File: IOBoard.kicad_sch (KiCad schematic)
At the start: 45 parts, among them J1 Conn_02x05_Odd_Even, J10 Conn_02x05_Odd_Even, J11 Conn_02x05_Odd_Even, J2 Conn_02x05_Odd_Even, J3 Conn_01x03, J4 Conn_01x03, J5 Conn_01x03, J6 Conn_01x03, J7 Conn_01x03, J8 Conn_01x03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

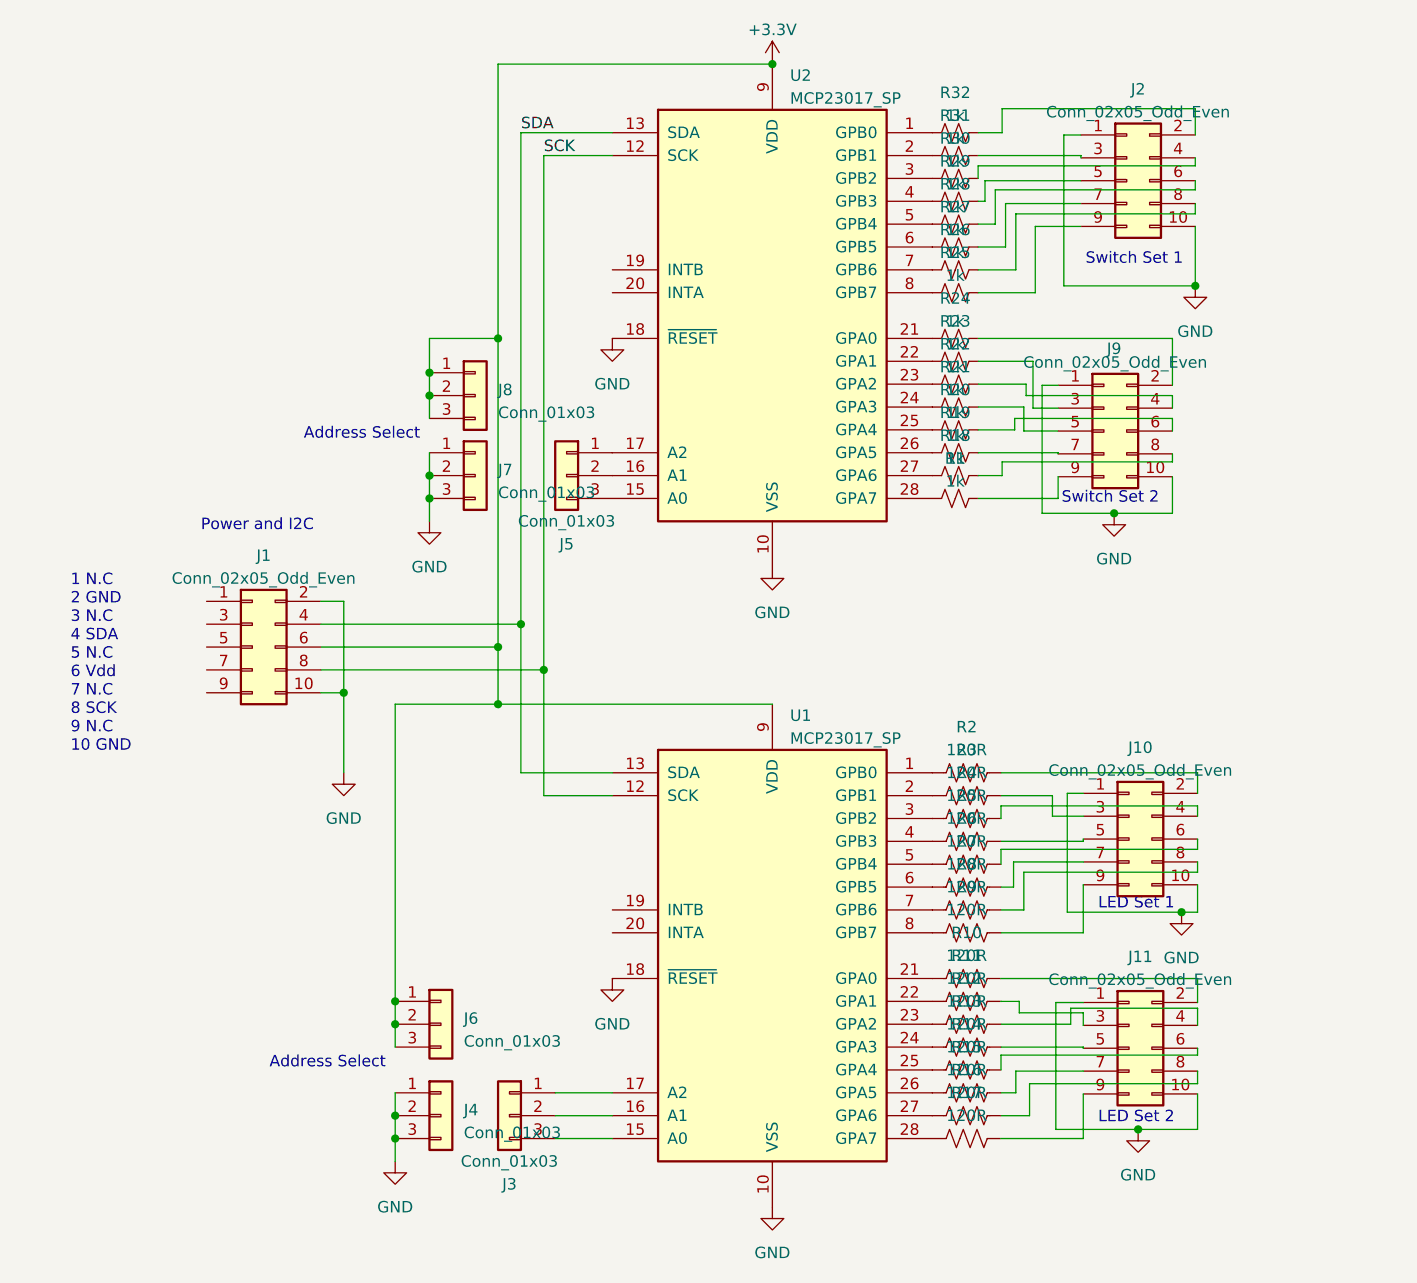
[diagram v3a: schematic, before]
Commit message: Fix schematic error and re-layout board.  Start a tray to hold board.
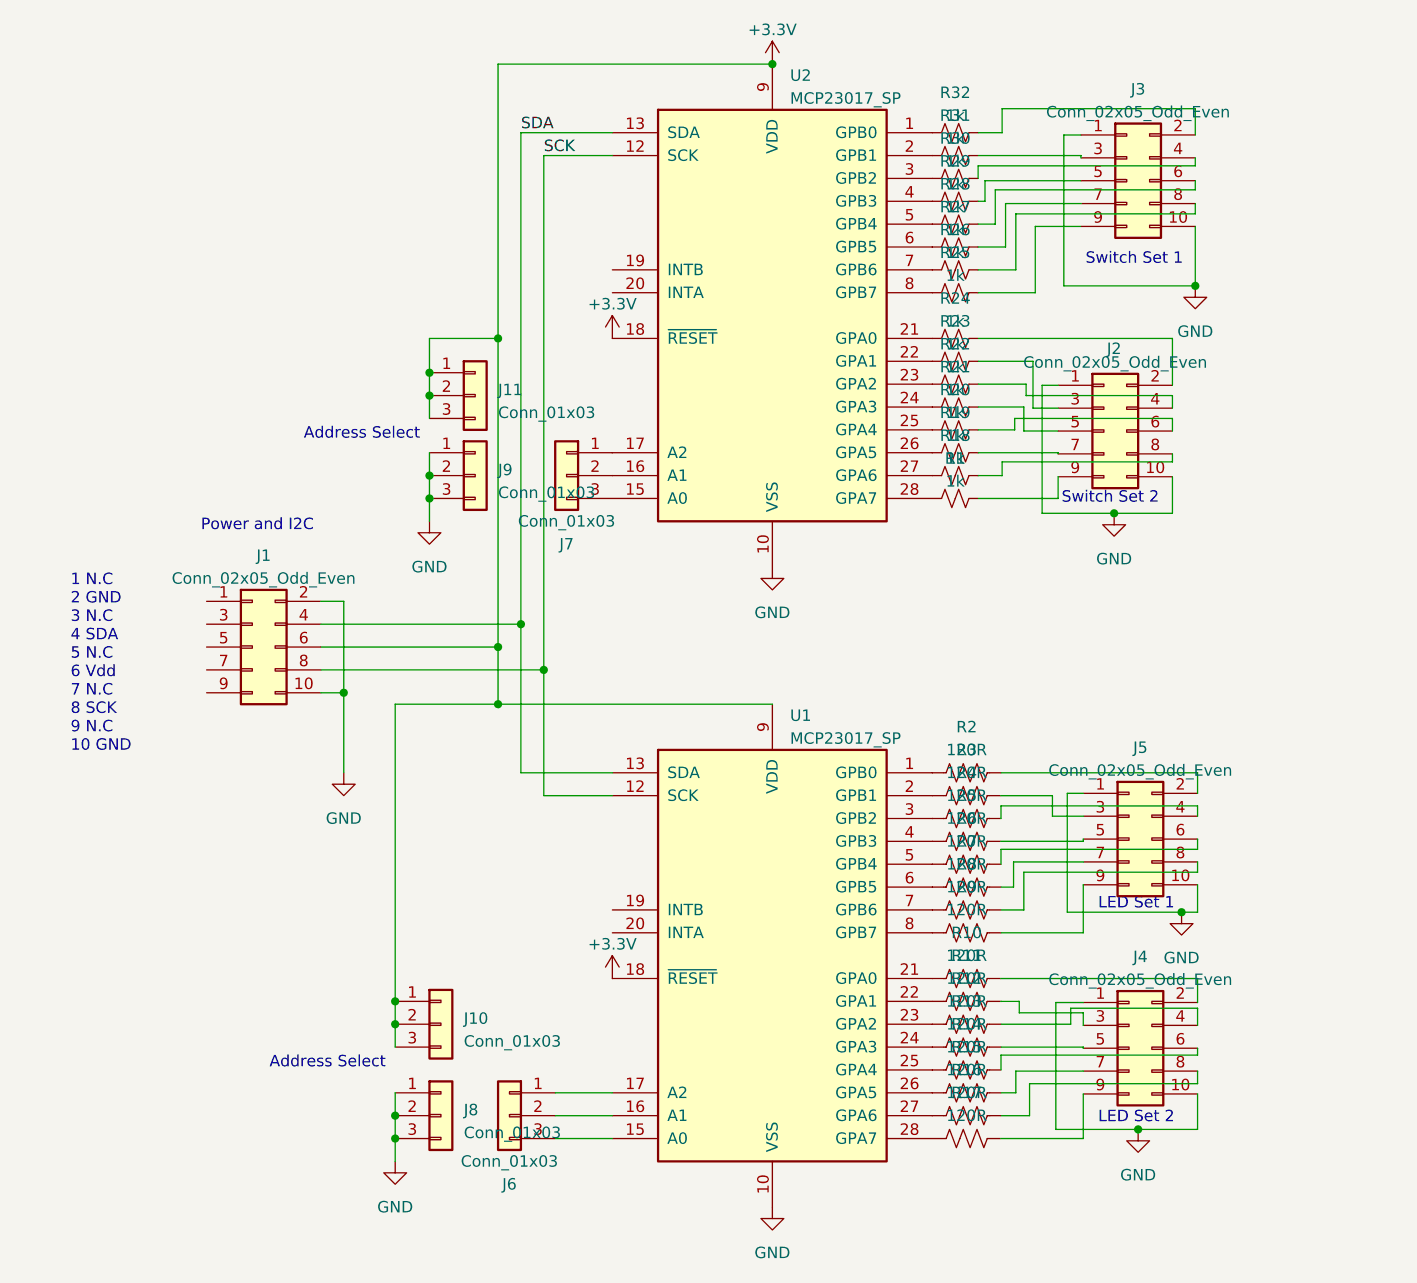
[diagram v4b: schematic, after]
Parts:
- J2: renamed from J9; footprint Connector_PinHeader_2.54mm:PinHeader_2x05_P2.54mm_Vertical -> Connector_PinHeader_2.54mm:PinHeader_2x05_P2.54mm_Horizontal
- J3: renamed from J2; footprint Connector_PinHeader_2.54mm:PinHeader_2x05_P2.54mm_Vertical -> Connector_PinHeader_2.54mm:PinHeader_2x05_P2.54mm_Horizontal
- J4: renamed from J11; footprint Connector_PinHeader_2.54mm:PinHeader_2x05_P2.54mm_Vertical -> Connector_PinHeader_2.54mm:PinHeader_2x05_P2.54mm_Horizontal
- J5: renamed from J10; footprint Connector_PinHeader_2.54mm:PinHeader_2x05_P2.54mm_Vertical -> Connector_PinHeader_2.54mm:PinHeader_2x05_P2.54mm_Horizontal
- renumbered J6 to J10, J8 to J11, J3 to J6, J5 to J7, J4 to J8, J7 to J9
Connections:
- net +3.3V: now also U1.18 (~{RESET}), U2.18 (~{RESET})
- net GND: no longer U1.18 (~{RESET}), U2.18 (~{RESET})
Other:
- title: 16 Switch, 16 LED I/O Board -> 32 GPIO Board
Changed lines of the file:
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@@
   (paper "A4")
   (title_block
-    (title "16 Switch, 16 LED I/O Board")
-    (date "9-Jul-2023")
-    (rev "-")
+    (title "32 GPIO Board")
+    (date "24-Jul-2023")
+    (rev "1")
   )
   (junction (at 76.2 71.12) (diameter 0) (color 0 0 0 0)
@@
   (symbol (lib_id "Connector_Generic:Conn_02x05_Odd_Even") (at 151.13 66.167 0) (unit 1)
     (in_bom yes) (on_board yes) (dnp no)
-    (property "Reference" "J9" (at 152.273 57.023 0)
+    (property "Reference" "J2" (at 152.273 57.023 0)
       (effects (font (size 1.27 1.27)))
     )
@@
       (effects (font (size 1.27 1.27)))
     )
-    (property "Footprint" "Connector_PinHeader_2.54mm:PinHeader_2x05_P2.54mm_Vertical" (at 151.13 66.167 0)
+    (property "Footprint" "Connector_PinHeader_2.54mm:PinHeader_2x05_P2.54mm_Horizontal" (at 151.13 66.167 0)
       (effects (font (size 1.27 1.27)) hide)
     )
@@
       (project "IOBoard"
         (path "/6176cf7e-07e6-4752-9af2-56387280742c"
-          (reference "J9") (unit 1)
+          (reference "J2") (unit 1)
         )
       )
@@
   (symbol (lib_id "Connector_Generic:Conn_01x03") (at 81.28 62.23 0) (unit 1)
     (in_bom yes) (on_board yes) (dnp no) (fields_autoplaced)
-    (property "Reference" "J8" (at 83.82 61.595 0)
+    (property "Reference" "J11" (at 83.82 61.595 0)
       (effects (font (size 1.27 1.27)) (justify left))
     )
@@
       (project "IOBoard"
         (path "/6176cf7e-07e6-4752-9af2-56387280742c"
-          (reference "J8") (unit 1)
+          (reference "J11") (unit 1)
         )
       )
@@
     )
   )
-  (symbol (lib_id "power:GND") (at 96.52 55.88 0) (unit 1)
-    (in_bom yes) (on_board yes) (dnp no) (fields_autoplaced)
-    (property "Reference" "#PWR03" (at 96.52 62.23 0)
-      (effects (font (size 1.27 1.27)) hide)
-    )
-    (property "Value" "GND" (at 96.52 60.96 0)
-      (effects (font (size 1.27 1.27)))
-    )
-    (property "Footprint" "" (at 96.52 55.88 0)
-      (effects (font (size 1.27 1.27)) hide)
-    )
-    (property "Datasheet" "" (at 96.52 55.88 0)
-      (effects (font (size 1.27 1.27)) hide)
-    )
-    (pin "1")
-    (instances
-      (project "IOBoard"
-        (path "/6176cf7e-07e6-4752-9af2-56387280742c"
-          (reference "#PWR03") (unit 1)
-        )
-      )
-    )
-  )
   (symbol (lib_id "power:GND") (at 154.94 143.764 0) (unit 1)
     (in_bom yes) (on_board yes) (dnp no) (fields_autoplaced)
@@
   (symbol (lib_id "Connector_Generic:Conn_01x03") (at 81.28 71.12 0) (unit 1)
     (in_bom yes) (on_board yes) (dnp no) (fields_autoplaced)
-    (property "Reference" "J7" (at 83.82 70.485 0)
+    (property "Reference" "J9" (at 83.82 70.485 0)
       (effects (font (size 1.27 1.27)) (justify left))
     )
@@
       (project "IOBoard"
         (path "/6176cf7e-07e6-4752-9af2-56387280742c"
-          (reference "J7") (unit 1)
+          (reference "J9") (unit 1)
         )
       )
@@
   (symbol (lib_id "Connector_Generic:Conn_02x05_Odd_Even") (at 153.67 38.354 0) (unit 1)
     (in_bom yes) (on_board yes) (dnp no) (fields_autoplaced)
-    (property "Reference" "J2" (at 154.94 28.194 0)
+    (property "Reference" "J3" (at 154.94 28.194 0)
       (effects (font (size 1.27 1.27)))
     )
@@
       (effects (font (size 1.27 1.27)))
     )
-    (property "Footprint" "Connector_PinHeader_2.54mm:PinHeader_2x05_P2.54mm_Vertical" (at 153.67 38.354 0)
+    (property "Footprint" "Connector_PinHeader_2.54mm:PinHeader_2x05_P2.54mm_Horizontal" (at 153.67 38.354 0)
       (effects (font (size 1.27 1.27)) hide)
     )
@@
       (project "IOBoard"
         (path "/6176cf7e-07e6-4752-9af2-56387280742c"
-          (reference "J2") (unit 1)
+          (reference "J3") (unit 1)
         )
       )
@@
     )
   )
+  (symbol (lib_id "power:+3.3V") (at 96.52 55.88 0) (unit 1)
+    (in_bom yes) (on_board yes) (dnp no) (fields_autoplaced)
+    (property "Reference" "#PWR03" (at 96.52 59.69 0)
+      (effects (font (size 1.27 1.27)) hide)
+    )
+    (property "Value" "+3.3V" (at 96.52 52.07 0)
+      (effects (font (size 1.27 1.27)))
+    )
+    (property "Footprint" "" (at 96.52 55.88 0)
+      (effects (font (size 1.27 1.27)) hide)
+    )
+    (property "Datasheet" "" (at 96.52 55.88 0)
+      (effects (font (size 1.27 1.27)) hide)
+    )
+    (pin "1")
+    (instances
+      (project "IOBoard"
+        (path "/6176cf7e-07e6-4752-9af2-56387280742c"
+          (reference "#PWR03") (unit 1)
+        )
+      )
+    )
+  )
   (symbol (lib_id "power:GND") (at 114.3 81.28 0) (unit 1)
     (in_bom yes) (on_board yes) (dnp no) (fields_autoplaced)
@@
   (symbol (lib_id "Connector_Generic:Conn_02x05_Odd_Even") (at 153.924 111.506 0) (unit 1)
     (in_bom yes) (on_board yes) (dnp no) (fields_autoplaced)
-    (property "Reference" "J10" (at 155.194 101.346 0)
+    (property "Reference" "J5" (at 155.194 101.346 0)
       (effects (font (size 1.27 1.27)))
     )
@@
       (effects (font (size 1.27 1.27)))
     )
-    (property "Footprint" "Connector_PinHeader_2.54mm:PinHeader_2x05_P2.54mm_Vertical" (at 153.924 111.506 0)
+    (property "Footprint" "Connector_PinHeader_2.54mm:PinHeader_2x05_P2.54mm_Horizontal" (at 153.924 111.506 0)
       (effects (font (size 1.27 1.27)) hide)
     )
@@
       (project "IOBoard"
         (path "/6176cf7e-07e6-4752-9af2-56387280742c"
-          (reference "J10") (unit 1)
+          (reference "J5") (unit 1)
         )
       )
@@
     )
   )
+  (symbol (lib_id "power:+3.3V") (at 96.52 127 0) (unit 1)
+    (in_bom yes) (on_board yes) (dnp no) (fields_autoplaced)
+    (property "Reference" "#PWR04" (at 96.52 130.81 0)
+      (effects (font (size 1.27 1.27)) hide)
+    )
+    (property "Value" "+3.3V" (at 96.52 123.19 0)
+      (effects (font (size 1.27 1.27)))
+    )
+    (property "Footprint" "" (at 96.52 127 0)
+      (effects (font (size 1.27 1.27)) hide)
+    )
+    (property "Datasheet" "" (at 96.52 127 0)
+      (effects (font (size 1.27 1.27)) hide)
+    )
+    (pin "1")
+    (instances
+      (project "IOBoard"
+        (path "/6176cf7e-07e6-4752-9af2-56387280742c"
+          (reference "#PWR04") (unit 1)
+        )
+      )
+    )
+  )
   (symbol (lib_id "Device:R_US") (at 135.89 132.08 270) (unit 1)
     (in_bom yes) (on_board yes) (dnp no) (fields_autoplaced)
@@
   (symbol (lib_id "Connector_Generic:Conn_02x05_Odd_Even") (at 153.924 134.747 0) (unit 1)
     (in_bom yes) (on_board yes) (dnp no) (fields_autoplaced)
-    (property "Reference" "J11" (at 155.194 124.587 0)
+    (property "Reference" "J4" (at 155.194 124.587 0)
       (effects (font (size 1.27 1.27)))
     )
@@
       (effects (font (size 1.27 1.27)))
     )
-    (property "Footprint" "Connector_PinHeader_2.54mm:PinHeader_2x05_P2.54mm_Vertical" (at 153.924 134.747 0)
+    (property "Footprint" "Connector_PinHeader_2.54mm:PinHeader_2x05_P2.54mm_Horizontal" (at 153.924 134.747 0)
       (effects (font (size 1.27 1.27)) hide)
     )
@@
       (project "IOBoard"
         (path "/6176cf7e-07e6-4752-9af2-56387280742c"
-          (reference "J11") (unit 1)
-        )
-      )
-    )
-  )
-  (symbol (lib_id "power:GND") (at 96.52 127 0) (unit 1)
-    (in_bom yes) (on_board yes) (dnp no) (fields_autoplaced)
-    (property "Reference" "#PWR04" (at 96.52 133.35 0)
-      (effects (font (size 1.27 1.27)) hide)
-    )
-    (property "Value" "GND" (at 96.52 132.08 0)
-      (effects (font (size 1.27 1.27)))
-    )
-    (property "Footprint" "" (at 96.52 127 0)
-      (effects (font (size 1.27 1.27)) hide)
-    )
-    (property "Datasheet" "" (at 96.52 127 0)
-      (effects (font (size 1.27 1.27)) hide)
-    )
-    (pin "1")
-    (instances
-      (project "IOBoard"
-        (path "/6176cf7e-07e6-4752-9af2-56387280742c"
-          (reference "#PWR04") (unit 1)
+          (reference "J4") (unit 1)
         )
       )
@@
   (symbol (lib_id "Connector_Generic:Conn_01x03") (at 77.47 142.24 0) (unit 1)
     (in_bom yes) (on_board yes) (dnp no) (fields_autoplaced)
-    (property "Reference" "J4" (at 80.01 141.605 0)
+    (property "Reference" "J8" (at 80.01 141.605 0)
       (effects (font (size 1.27 1.27)) (justify left))
     )
@@
       (project "IOBoard"
         (path "/6176cf7e-07e6-4752-9af2-56387280742c"
-          (reference "J4") (unit 1)
+          (reference "J8") (unit 1)
         )
       )
@@
   (symbol (lib_id "Connector_Generic:Conn_01x03") (at 77.47 132.08 0) (unit 1)
     (in_bom yes) (on_board yes) (dnp no) (fields_autoplaced)
-    (property "Reference" "J6" (at 80.01 131.445 0)
+    (property "Reference" "J10" (at 80.01 131.445 0)
       (effects (font (size 1.27 1.27)) (justify left))
     )
@@
       (project "IOBoard"
         (path "/6176cf7e-07e6-4752-9af2-56387280742c"
-          (reference "J6") (unit 1)
+          (reference "J10") (unit 1)
         )
       )
@@
   (symbol (lib_id "Connector_Generic:Conn_01x03") (at 91.44 71.12 0) (mirror y) (unit 1)
     (in_bom yes) (on_board yes) (dnp no)
-    (property "Reference" "J5" (at 91.44 78.74 0)
+    (property "Reference" "J7" (at 91.44 78.74 0)
       (effects (font (size 1.27 1.27)))
     )
@@
       (project "IOBoard"
         (path "/6176cf7e-07e6-4752-9af2-56387280742c"
-          (reference "J5") (unit 1)
+          (reference "J7") (unit 1)
         )
       )
@@
   (symbol (lib_id "Connector_Generic:Conn_01x03") (at 85.09 142.24 0) (mirror y) (unit 1)
     (in_bom yes) (on_board yes) (dnp no)
-    (property "Reference" "J3" (at 85.09 149.86 0)
+    (property "Reference" "J6" (at 85.09 149.86 0)
       (effects (font (size 1.27 1.27)))
     )
@@
       (project "IOBoard"
         (path "/6176cf7e-07e6-4752-9af2-56387280742c"
-          (reference "J3") (unit 1)
-        )
-      )
+          (reference "J6") (unit 1)
+        )
+      )
